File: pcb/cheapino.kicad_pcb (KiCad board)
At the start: 2 copper layers, 151.1 x 95.1 mm, 65 parts, among them K1 SW_Push, K10 SW_Push, K11 SW_Push, K12 SW_Push, K13 SW_Push, K14 SW_Push, K15 SW_Push, K16 SW_Push, K17 SW_Push, K18 SW_Push, K19 K19, K2 SW_Push, K20 K20, K21 K21, K3 SW_Push, K4 SW_Push, K5 SW_Push, K6 SW_Push, K7 SW_Push, K8 SW_Push, K9 SW_Push, U1 RP2040-Zero

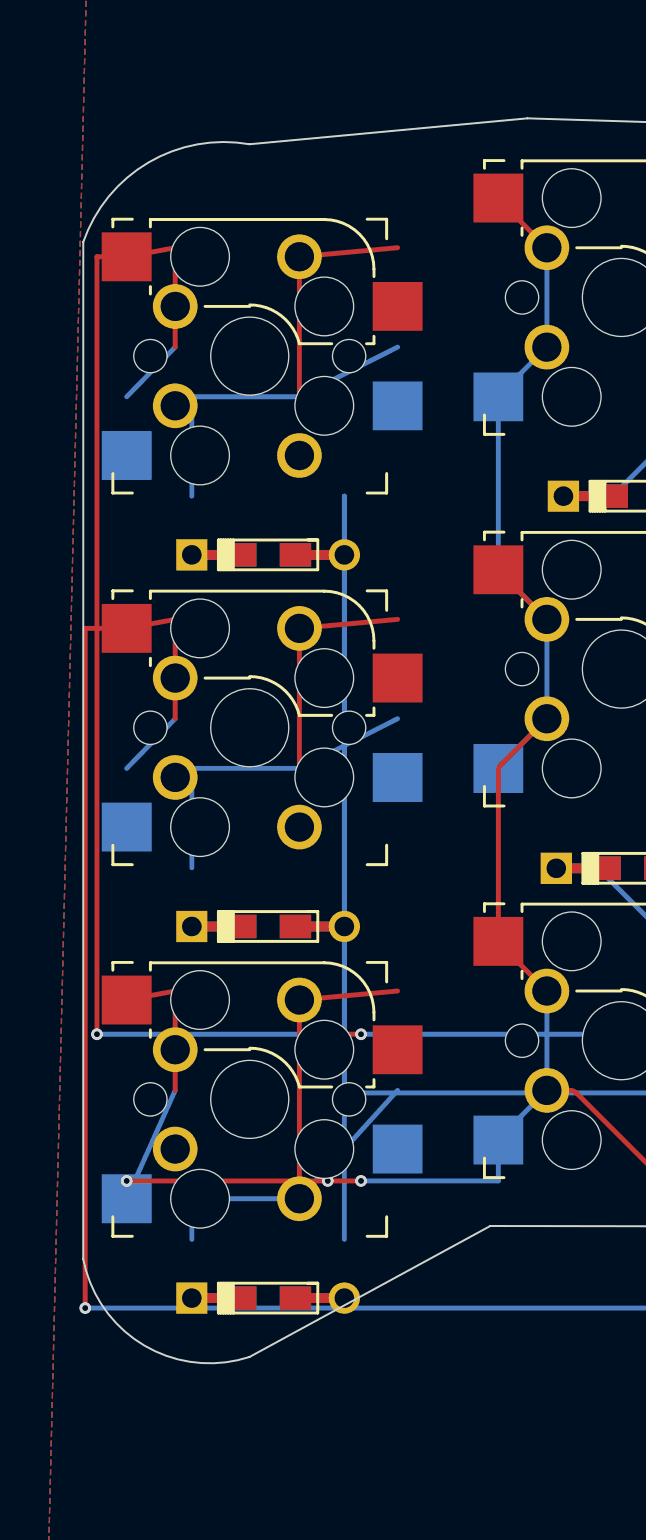
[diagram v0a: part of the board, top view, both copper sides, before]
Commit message: Improve left outline: more D24 clearance + softer curves, closed shape
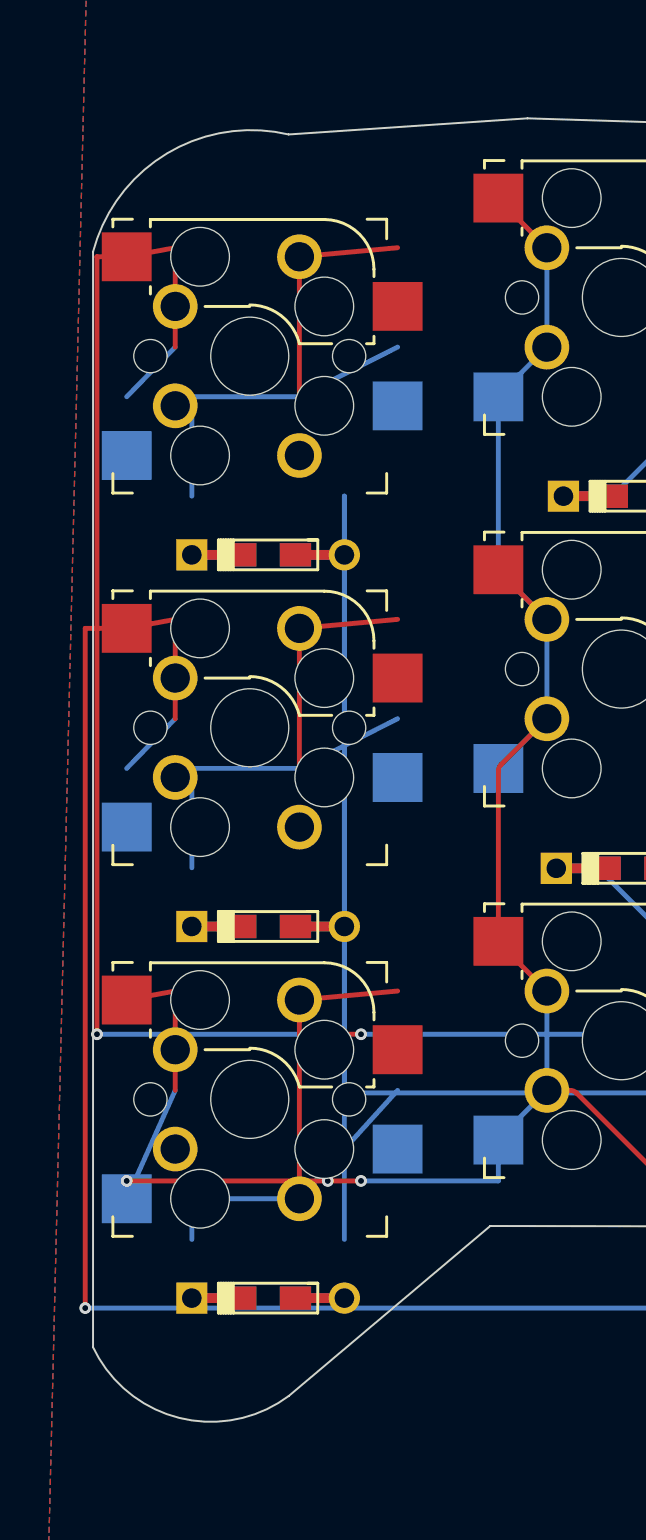
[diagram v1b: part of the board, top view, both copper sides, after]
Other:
- board size 151.1 x 95.1 mm -> 150.6 x 95.1 mm
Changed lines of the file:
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@@
 	(gr_line
+		(start 62.3062 117.804489)
+		(end 52.0 126.5)
+		(stroke
+			(width 0.1)
+			(type solid)
+		)
+		(layer "Edge.Cuts")
+	)
+	(gr_arc
+		(start 52.0 126.5)
+		(mid 46.0 127.5)
+		(end 42.0 124.0)
+		(stroke
+			(width 0.1)
+			(type solid)
+		)
+		(layer "Edge.Cuts")
+	)
+	(gr_line
+		(start 42.0 124.0)
+		(end 42.0 68.0)
+		(stroke
+			(width 0.1)
+			(type solid)
+		)
+		(layer "Edge.Cuts")
+	)
+	(gr_arc
+		(start 42.0 68.0)
+		(mid 45.0 63.5)
+		(end 52.0 62.0)
+		(stroke
+			(width 0.1)
+			(type solid)
+		)
+		(layer "Edge.Cuts")
+	)
+	(gr_line
+		(start 52.0 62.0)
+		(end 64.2112 61.175373)
+		(stroke
+			(width 0.1)
+			(type solid)
+		)
+		(layer "Edge.Cuts")
+	)
+(gr_line
 		(start 62.3062 117.804489)
 		(end 77.241392 117.828012)
@@
 		(stroke
 			(width 0.1)
-			(type solid)
-		)
-		(layer "Edge.Cuts")
-	)
-(gr_line
-		(start 62.3062 117.804489)
-		(end 50.0 124.5)
-		(stroke
-			(width 0.1)
-			(type solid)
-		)
-		(layer "Edge.Cuts")
-	)
-	(gr_arc
-		(start 50.0 124.5)
-		(mid 44.0 123.5)
-		(end 41.5 119.5)
-		(stroke
-			(width 0.1)
-			(type solid)
-		)
-		(layer "Edge.Cuts")
-	)
-	(gr_line
-		(start 41.5 119.5)
-		(end 41.5 67.5)
-		(stroke
-			(width 0.1)
-			(type solid)
-		)
-		(layer "Edge.Cuts")
-	)
-	(gr_arc
-		(start 41.5 67.5)
-		(mid 44.0 64.0)
-		(end 50.0 62.5)
-		(stroke
-			(width 0.1)
-			(type solid)
-		)
-		(layer "Edge.Cuts")
-	)
-	(gr_line
-		(start 50.0 62.5)
-		(end 64.2112 61.175373)
-		(stroke
-			(width 0.1)

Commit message: test
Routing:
- net COL_1: track 363.7 -> 379.9 mm
- net Net-(D22-K): track 28.4 -> 12.2 mm
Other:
- board size 150.6 x 95.1 mm -> 152.2 x 95.1 mm

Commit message: Connect Edge.Cuts segments to form closed board outline
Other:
- outline, holes or cut-outs redrawn
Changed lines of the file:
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@@
+			(type solid)
+		)
+		(		(gr_line
+		(start 40.5 121.0)
+		(end 40.476394 121.485718)
+		(stroke
+			(width 0.1)
+			(type solid)
+		)
+		(layer "Edge.Cuts")
+	)
+(gr_line
+		(start 40.5 121.0)
+		(end 40.476394 121.485718)
+		(stroke
+			(width 0.1)
 			(type solid)
 		)
@@
 	)
 	(gr_line
+		(start 42.0 123.25)
+		(end 42.532404 123.238238)
+		(stroke
+			(width 0.1)
+			(type solid)
+		)
+		(layer "Edge.Cuts")
+	)
+	(gr_line
+		(start 40.5 66.0)
+		(end 40.457115 65.654282)
+		(stroke
+			(width 0.1)
+			(type solid)
+		)
+		(layer "Edge.Cuts")
+	)
+	(gr_line
+		(start 41.385249 64.709038)
+		(end 41.75 64.75)
+		(stroke
+			(width 0.1)
+			(type solid)
+		)
+		(layer "Edge.Cuts")
+	)
+	(gr_line
+		(start 59.444196 63.463643)
+		(end 59.445056 63.115664)
+		(stroke
+			(width 0.1)
+			(type solid)
+		)
+		(layer "Edge.Cuts")
+	)
+	(gr_line
+		(start 60.739597 61.922065)
+		(end 61.25 61.573308)
+		(stroke
+			(width 0.1)
+			(type solid)
+		)
+		(layer "Edge.Cuts")
+	)
+	(gr_line
+		(start 59.483081 121.0)
+		(end 59.395416 121.333957)
+		(stroke
+			(width 0.1)
+			(type solid)
+		)
+		(layer "Edge.Cuts")
+	)
+	(gr_line
+		(start 61.5 117.75)
+		(end 62.0 117.828012)
+		(stroke
+			(width 0.1)
+			(type solid)
+		)
+		(layer "Edge.Cuts")
+	)
+layer "Edge.Cuts")
+	)
+	(gr_line

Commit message: Fix corrupted Edge.Cuts S-expression so board loads again
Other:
- outline, holes or cut-outs redrawn
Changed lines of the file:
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@@
-			(type solid)
-		)
-		(		(gr_line
-		(start 40.5 121.0)
-		(end 40.476394 121.485718)
-		(stroke
-			(width 0.1)
 			(type solid)
 		)
 		(layer "Edge.Cuts")
 	)
-(gr_line
+	(gr_line
 		(start 40.5 121.0)
 		(end 40.476394 121.485718)
@@
 		(layer "Edge.Cuts")
 	)
-layer "Edge.Cuts")
-	)
 	(gr_line

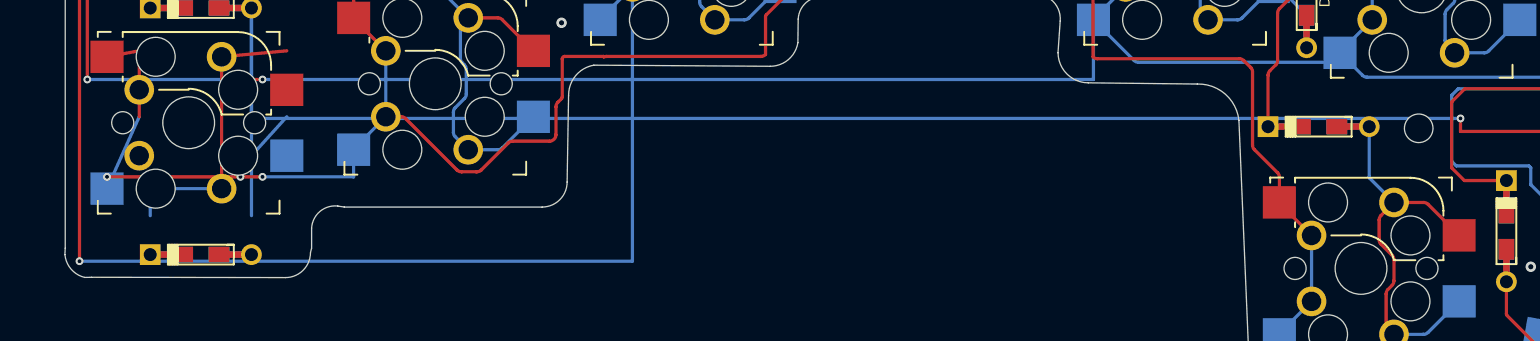
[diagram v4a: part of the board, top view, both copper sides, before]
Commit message: Remove long traces that crossed the empty board cutout (ROW_4, COL_1, COL_2)
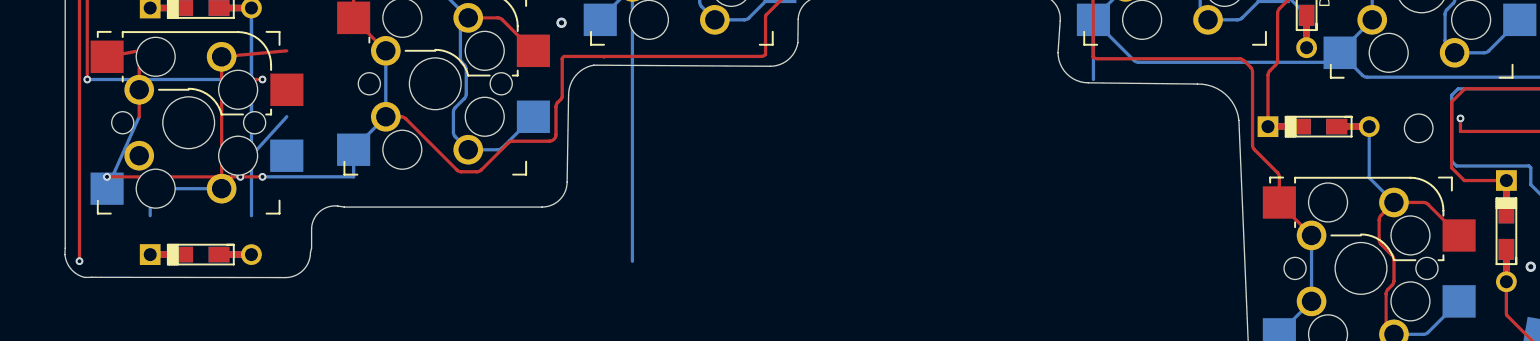
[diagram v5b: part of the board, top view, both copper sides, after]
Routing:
- net ROW_4: track 248.5 -> 155.3 mm
- net COL_1: track 379.9 -> 315.9 mm
- net COL_2: track 378.5 -> 335.9 mm
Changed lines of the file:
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@@
-	)
-	(segment
-		(start 41.6 122)
-		(end 84.2 122)
-		(width 0.25)
-		(layer "B.Cu")
-		(net "COL_2")
 	)
 	(segment
@@
 	)
 	(segment
-		(start 55.7 108)
-		(end 119.72 108)
-		(width 0.25)
-		(layer "B.Cu")
-		(net "COL_1")
-	)
-	(segment
 		(start 122.1994 95.7834)
 		(end 122.1994 100.8634)
@@
 		(width 0.25)
 		(layer "B.Cu")
-		(net "ROW_4")
-	)
-	(segment
-		(start 54.85 111)
-		(end 148 111)
-		(width 0.25)
-		(layer "B.Cu")

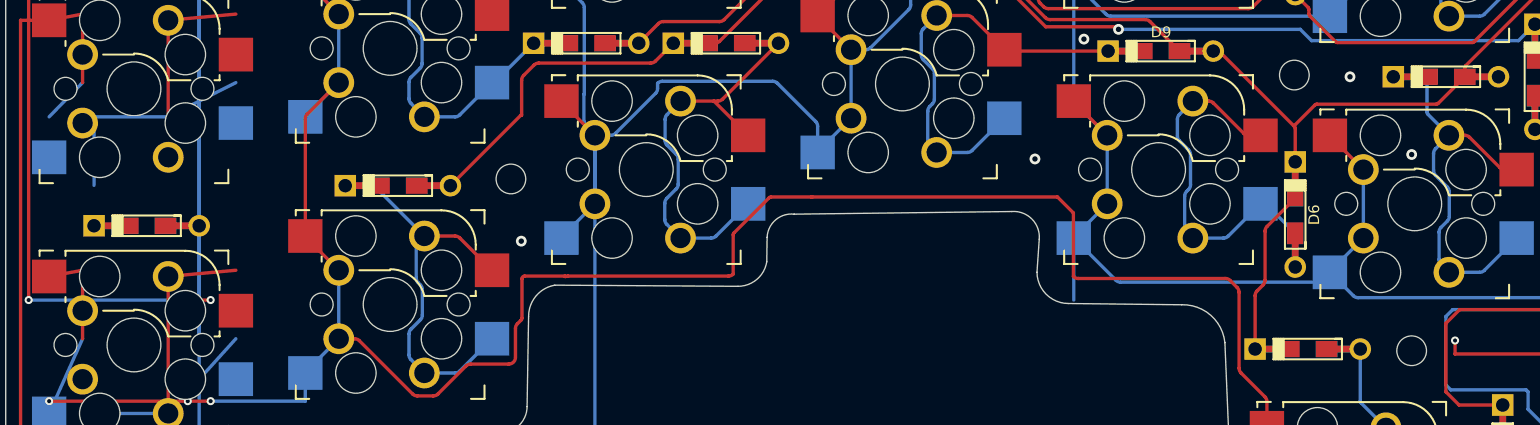
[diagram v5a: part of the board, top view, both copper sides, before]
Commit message: Re-route ROW_4, COL_1, COL_2 above cutout so traces stay on the board
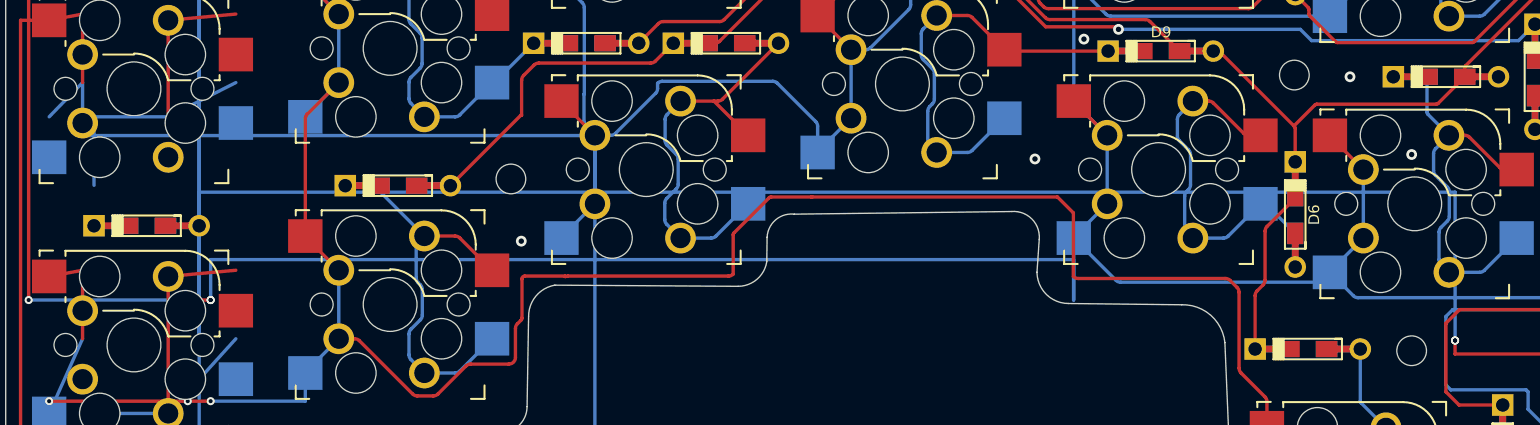
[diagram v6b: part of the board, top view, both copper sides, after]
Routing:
- net ROW_4: track 155.3 -> 270.5 mm, vias 4 -> 5
- net COL_1: track 315.9 -> 385.9 mm, vias 5 -> 6
- net COL_2: track 335.9 -> 377.8 mm
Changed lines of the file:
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@@
+		(net "ROW_4")
+	)
+		(segment
+		(start 54.85 111.0)
+		(end 54.85 100.0)
+		(width 0.25)
+		(layer "B.Cu")
 		(net "ROW_4")
 	)
 	(segment
+		(start 54.85 100.0)
+		(end 148.0 100.0)
+		(width 0.25)
+		(layer "B.Cu")
+		(net "ROW_4")
+	)
+	(segment
+		(start 148.0 100.0)
+		(end 148.0 111.0)
+		(width 0.25)
+		(layer "B.Cu")
+		(net "ROW_4")
+	)
+	(via
+		(at 148.0 111.0)
+		(size 0.6)
+		(drill 0.3)
+		(layers "F.Cu" "B.Cu")
+		(net "ROW_4")
+	)
+	(via
+		(at 55.7 108.0)
+		(size 0.6)
+		(drill 0.3)
+		(layers "F.Cu" "B.Cu")
+		(net "COL_1")
+	)
+	(segment
+		(start 55.7 108.0)
+		(end 55.7 105.0)
+		(width 0.25)
+		(layer "B.Cu")
+		(net "COL_1")
+	)
+	(segment
+		(start 55.7 105.0)
+		(end 119.7 105.0)
+		(width 0.25)
+		(layer "B.Cu")
+		(net "COL_1")
+	)
+	(segment
+		(start 119.7 105.0)
+		(end 119.7 108.0)
+		(width 0.25)
+		(layer "B.Cu")
+		(net "COL_1")
+	)
+	(segment
+		(start 46.2 91.87)
+		(end 46.2 95.8)
+		(width 0.25)
+		(layer "B.Cu")
+		(net "COL_2")
+	)
+	(segment
+		(start 46.2 95.8)
+		(end 84.2 95.8)
+		(width 0.25)
+		(layer "B.Cu")
+		(net "COL_2")
+	)
+(segment
 		(start 54.85 118.49)
 		(end 54.85 80.49)

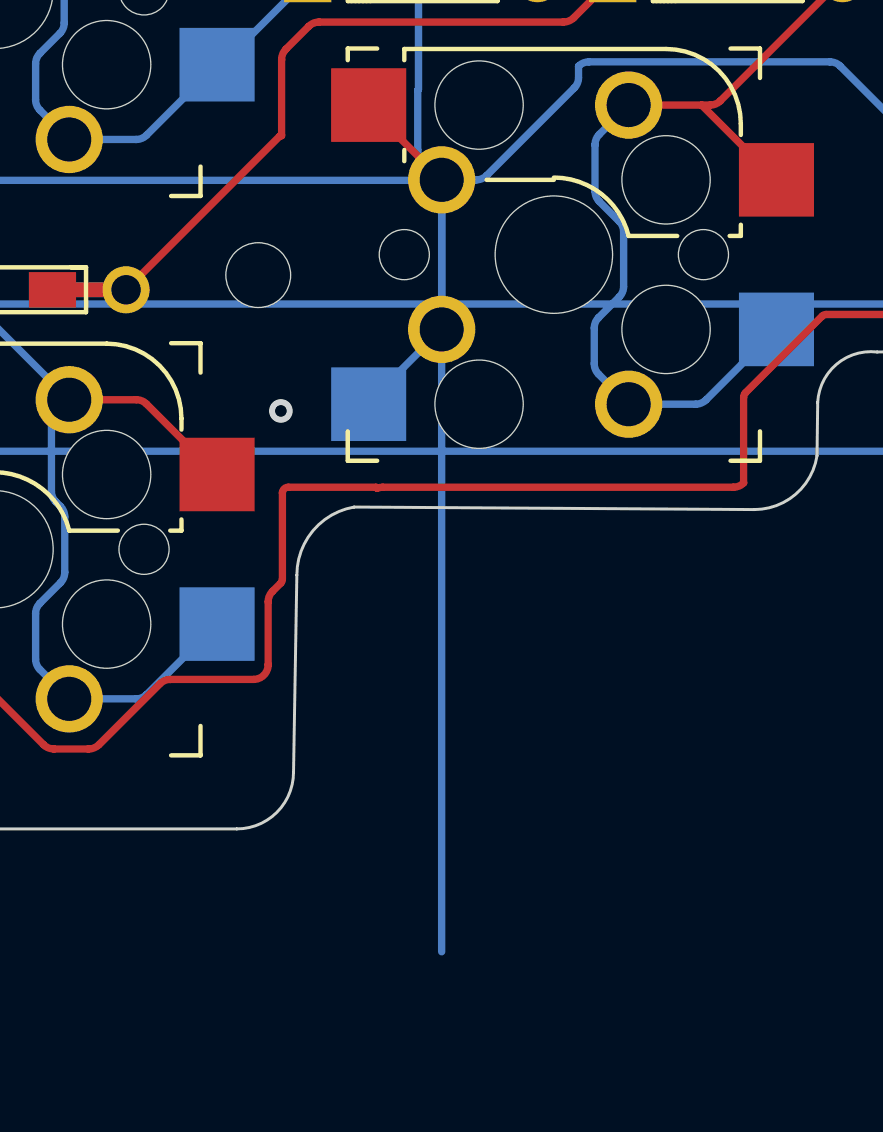
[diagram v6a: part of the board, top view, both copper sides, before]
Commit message: Trim COL_2 vertical so it no longer extends into the cutout void
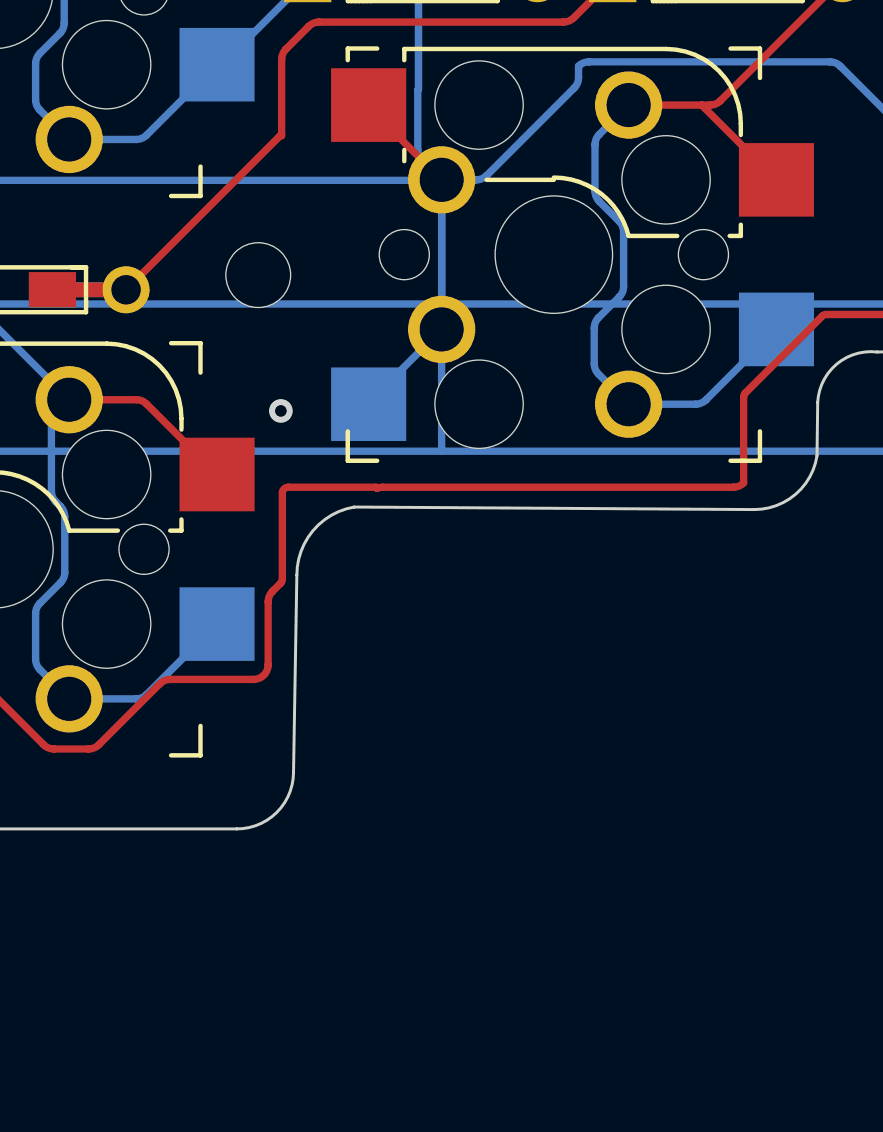
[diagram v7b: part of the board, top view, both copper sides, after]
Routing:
- net COL_2: track 377.8 -> 360.8 mm
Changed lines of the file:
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@@
 	)
 	(segment
-		(start 84.2 122)
+		(start 84.2 105)
 		(end 84.2 95.8)
 		(width 0.25)
